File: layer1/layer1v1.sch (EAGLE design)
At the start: 7 parts, among them U1 microSD, U2 DS3234

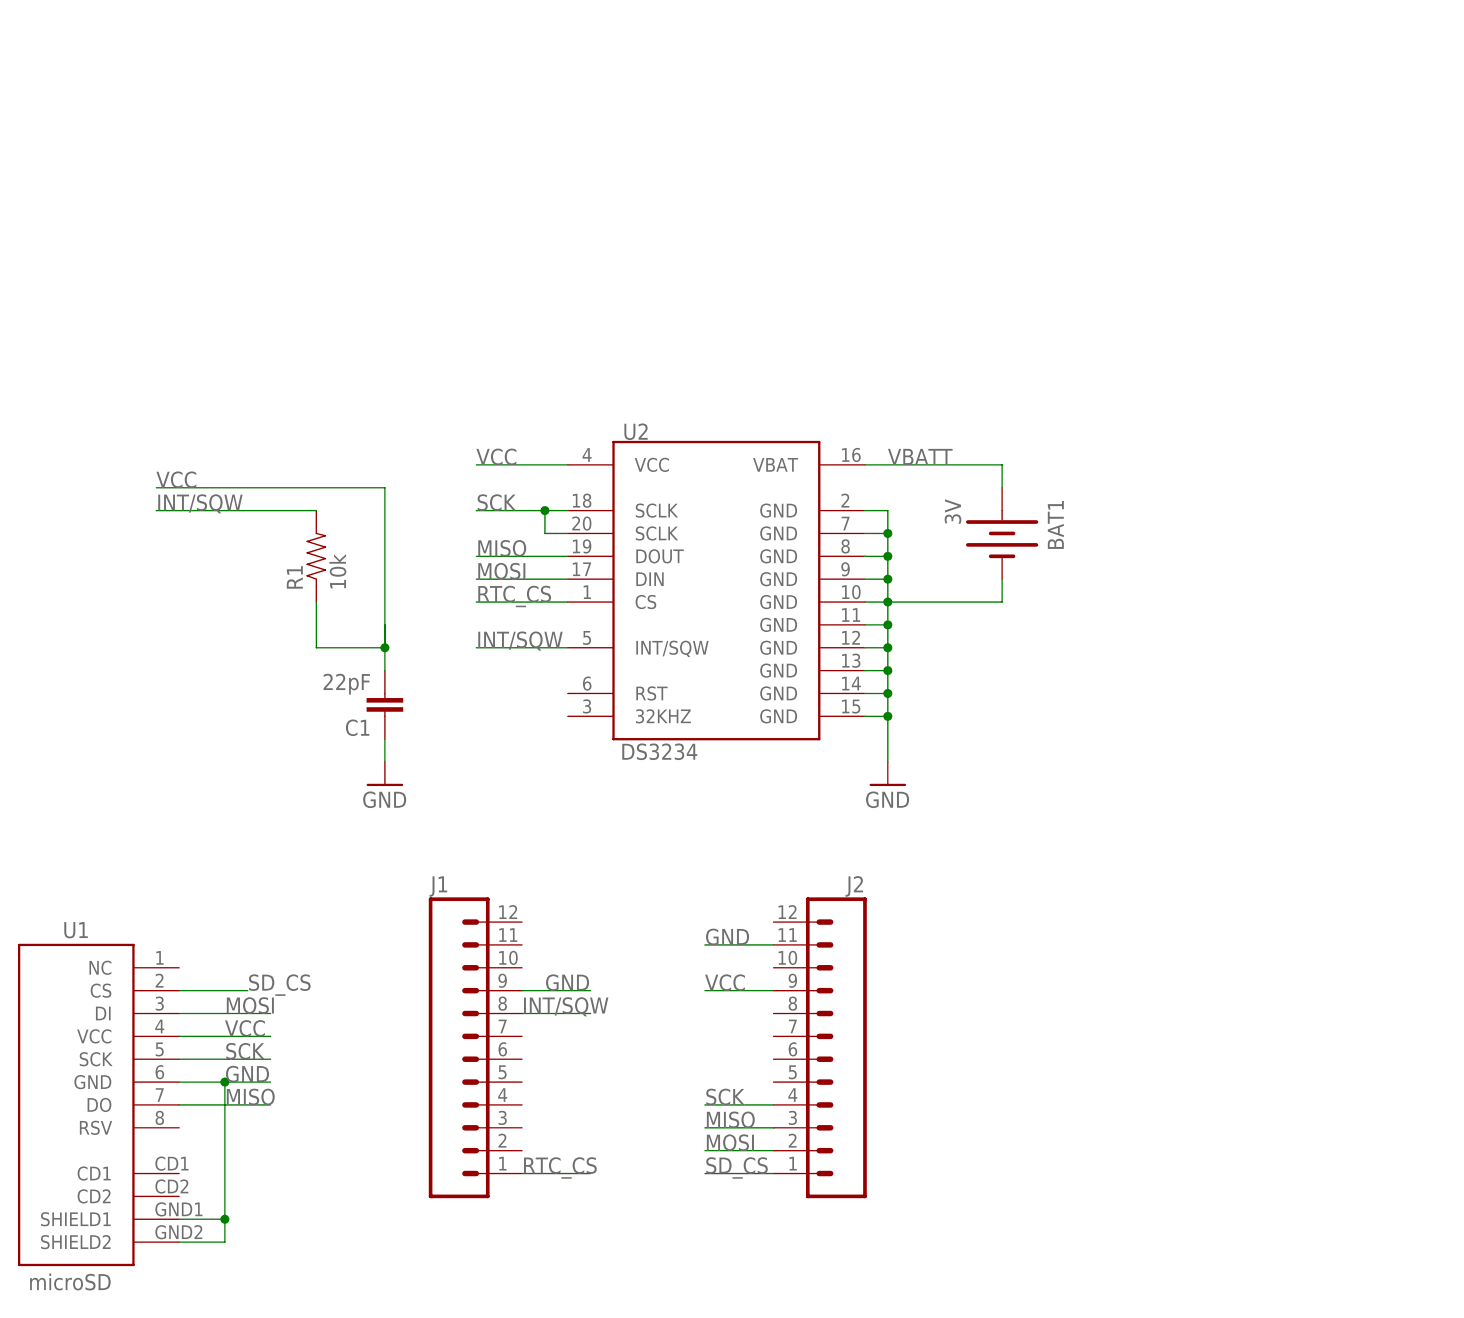
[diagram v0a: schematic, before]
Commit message: added batteri connection to board
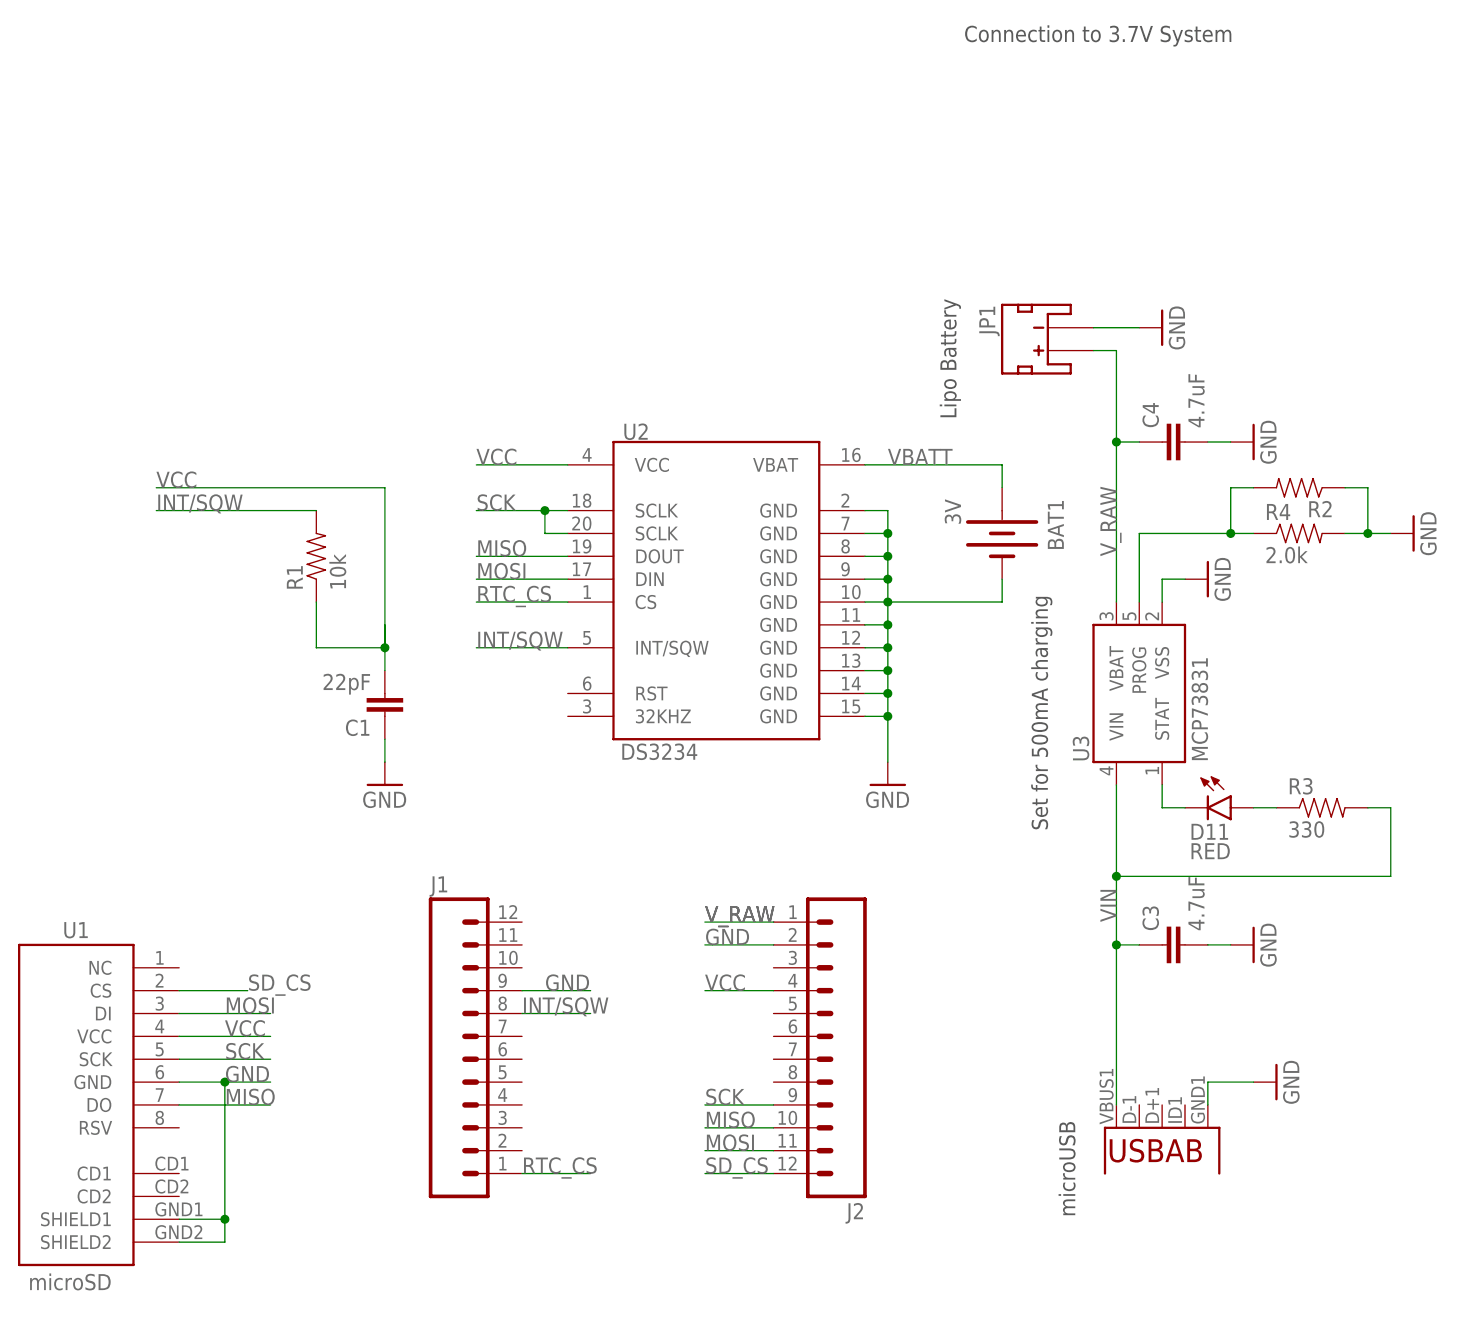
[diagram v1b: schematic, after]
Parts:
- added C3, C4: 4.7uF, SparkFun-Capacitors:4.7UF-6.3V-10%(0603)0603
- added D11: RED, SparkFun-LED:LED-RED0603
- added JP1: JST, SparkFun-Connectors:JST_2MM_MALE
- added JP9: Micro USB, SparkFun-Connectors:USB-ABCONN-11794
- added R2: (no value), SparkFun-Resistors:RESISTORPTH-1/4W-VERT-KIT
- added R3: 330, SparkFun-Resistors:330OHM1/10W1%(0603)
- added R4: 2.0k, SparkFun-Resistors:2.0KOHM1/10W5%(0603)
- added U3: MCP73831, SparkFun-PowerIC:MCP73831
- J1, J2: device SparkFun-Connectors:M12LOCK -> SparkFun-Connectors:M12PTH
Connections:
- new net N$3: D11.A, R3.1
- new net PROG: R2.2, R4.1, U3.PROG
- new net STAT: D11.C, U3.STAT
- new net VIN: C3.1, JP9.VBUS, R3.2, U3.VIN
- new net V_RAW: C4.1, J2.1, JP1.+, U3.VBAT
- net GND: now also C3.2, C4.2, J2.2, JP1.-, JP9.GND, R2.1, R4.2, U3.VSS; no longer J2.11
- net MISO: now also J2.10; no longer J2.3
- net MOSI: now also J2.11; no longer J2.2
- net SCK: now also J2.9; no longer J2.4
- net SD_CS: now also J2.12; no longer J2.1
- net VCC: now also J2.4; no longer J2.9
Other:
- note added: "Connection to 3.7V System"
- note added: "Lipo Battery"
- note added: "Set for 500mA charging"
- note added: "microUSB"
- moved on the sheet: J2
